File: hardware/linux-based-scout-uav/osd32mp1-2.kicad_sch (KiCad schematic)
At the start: 1 part, among them U1 OSD32MP157C-512M-IAA

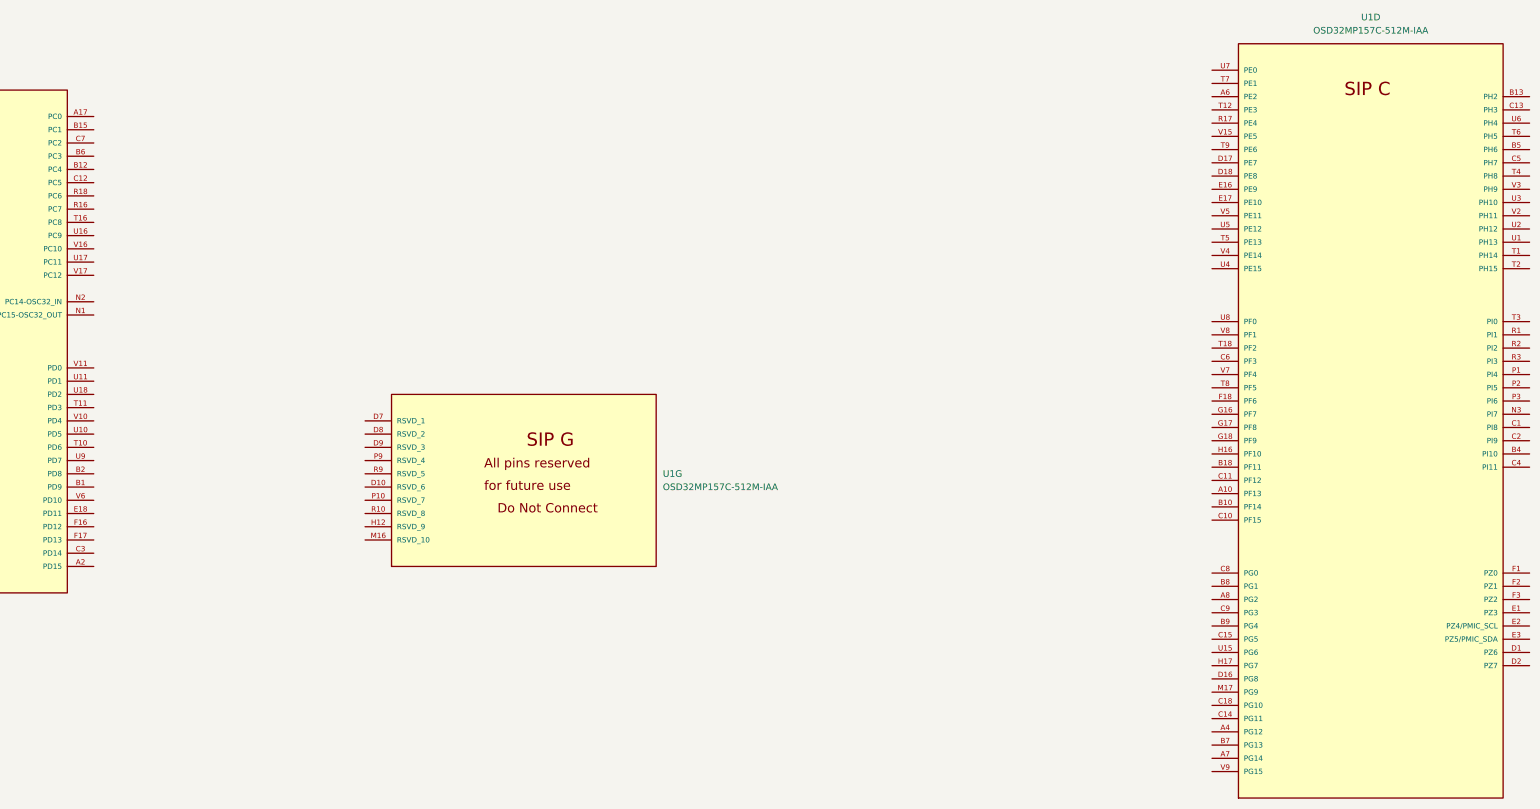
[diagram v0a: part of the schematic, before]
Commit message: Updates (Schematic, Readme, doc)
Updates to Schematic capture, README file and doc files.
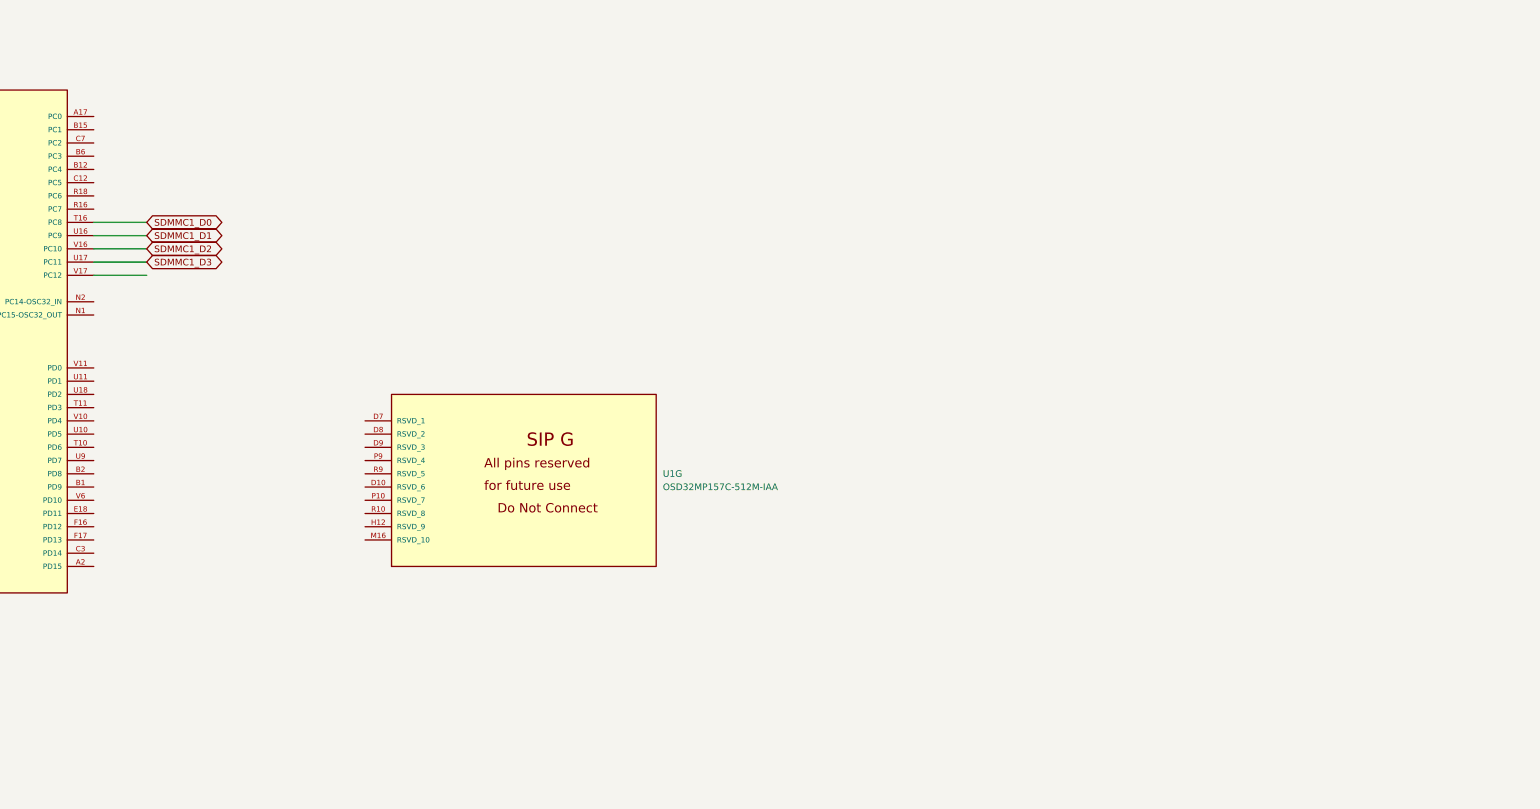
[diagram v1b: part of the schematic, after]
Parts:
- removed unit 4 of U1
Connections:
- net SDMMC1_D0: now reaches U1.T16 (PC8)
- net SDMMC1_D1: now reaches U1.U16 (PC9)
- net SDMMC1_D3: now reaches U1.U17 (PC11)
- net SDMMC1_D2: now reaches U1.V16 (PC10)

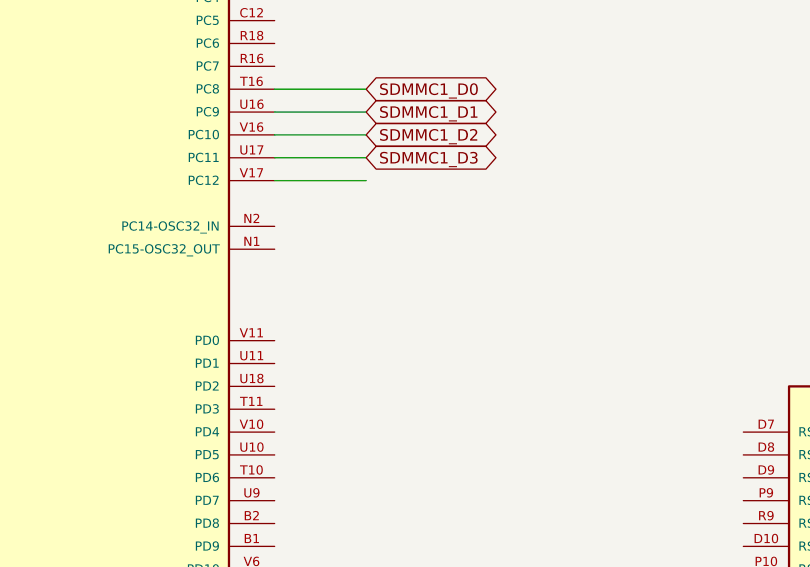
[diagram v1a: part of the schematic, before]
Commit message: Updates (schematic, readme, doc files, device tree)
Updates to schematic, readme file and doc files.
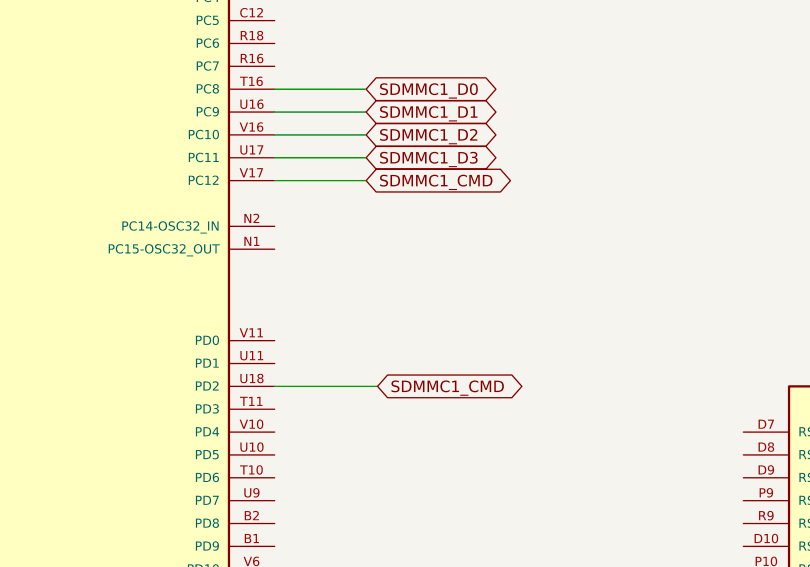
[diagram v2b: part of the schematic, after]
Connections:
- net SDMMC1_CMD: now reaches U1.U18 (PD2)
- net SDMMC1_CMD: now also U1.V17 (PC12)
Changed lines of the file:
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@@
 	(generator "eeschema")
 	(generator_version "8.0")
-	(paper "A4")
+	(paper "A3")
+	(wire
+		(pts
+			(xy 241.3 97.79) (xy 252.73 97.79)
+		)
+		(stroke
+			(width 0)
+			(type default)
+		)
+	)
 	(wire
 		(pts
@@
 			(width 0)
 			(type default)
+		)
+	)
+	(global_label "SDMMC1_CMD"
+		(shape bidirectional)
+		(at 251.46 74.93 0)
+		(fields_autoplaced yes)
+		(effects
+			(font
+				(size 1.27 1.27)
+			)
+			(justify left)
+		)
+		(property "Intersheetrefs" "${INTERSHEET_REFS}"
+			(at 268.3773 74.93 0)
+			(show_name yes)
+			(effects
+				(font
+					(size 1.27 1.27)
+				)
+				(justify left)
+				(hide yes)
+			)
 		)
 	)
@@
 			(effects
 				(font
+					(size 1.27 1.27)
+				)
+				(justify left)
+				(hide yes)
+			)
+		)
+	)
+	(global_label "SDMMC1_CMD"
+		(shape bidirectional)
+		(at 252.73 97.79 0)
+		(fields_autoplaced yes)
+		(effects
+			(font
+				(size 1.27 1.27)
+			)
+			(justify left)
+		)
+		(property "Intersheetrefs" "${INTERSHEET_REFS}"
+			(at 269.6473 97.79 0)
+			(show_name yes)
+			(effects
+				(font

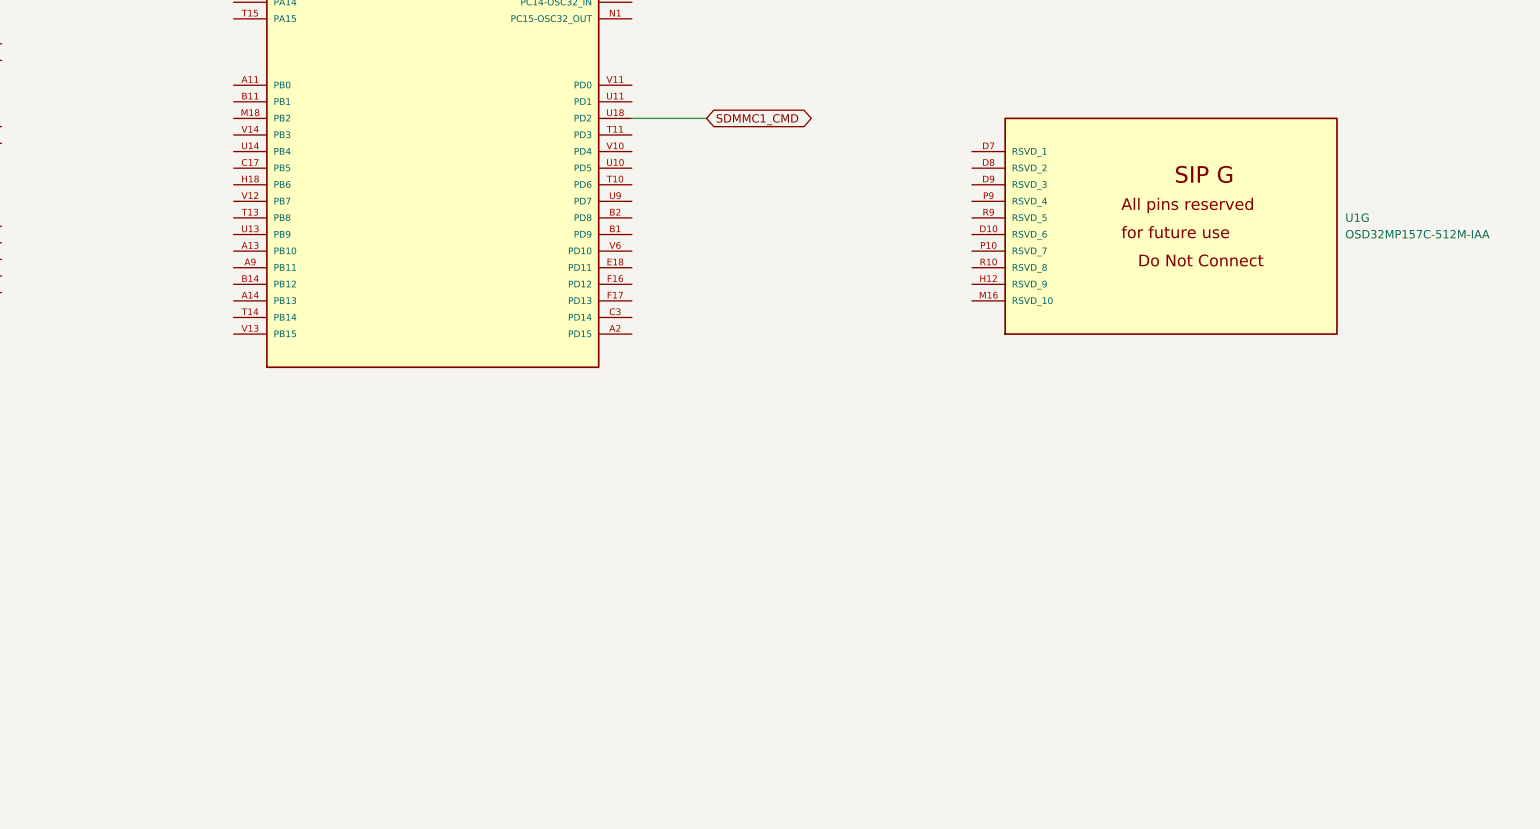
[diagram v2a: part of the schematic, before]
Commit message: schematic update
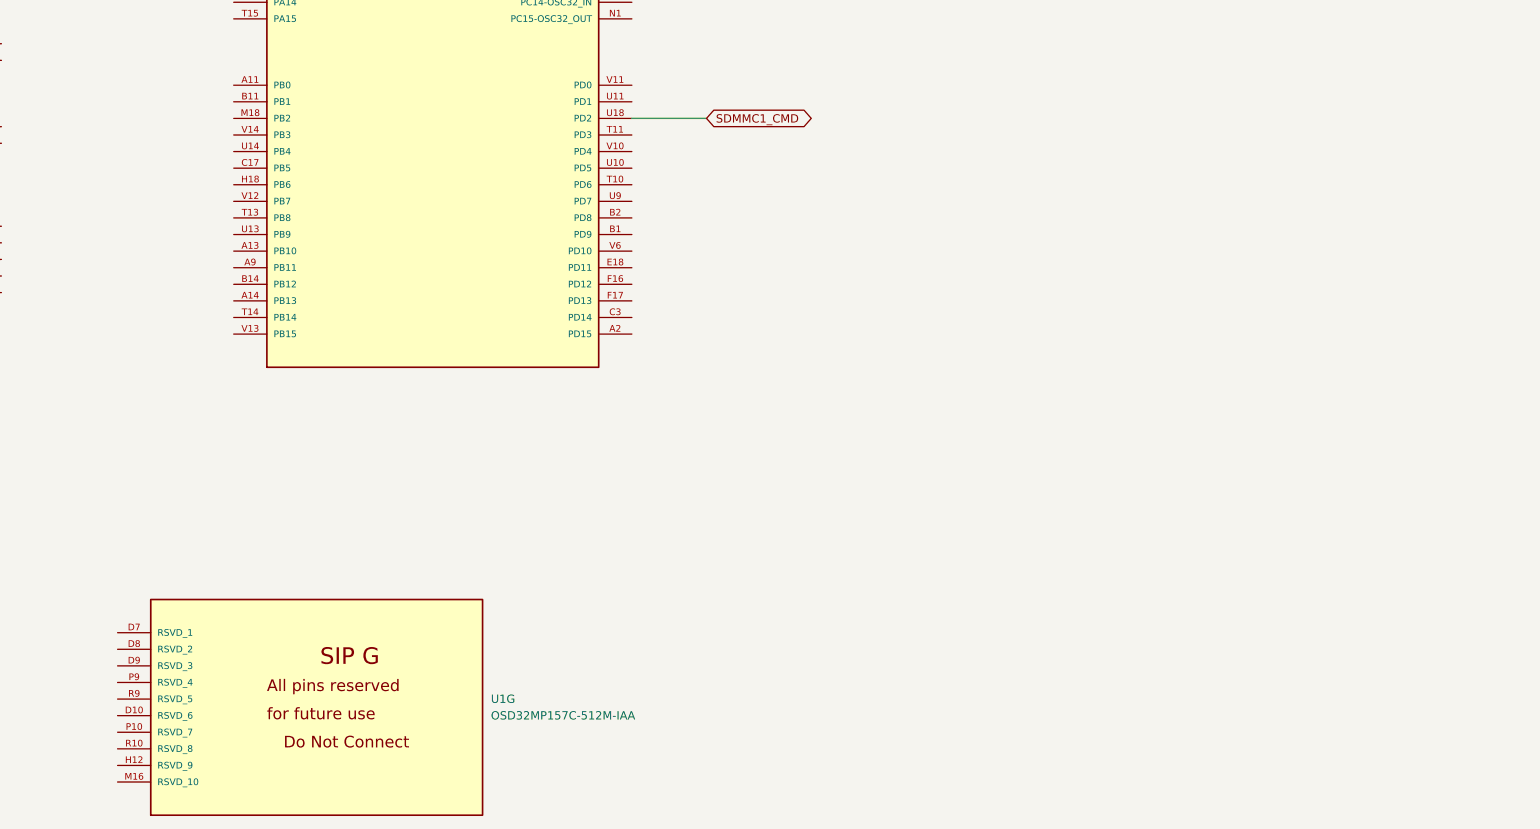
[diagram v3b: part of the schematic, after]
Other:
- moved on the sheet: U1G
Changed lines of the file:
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@@
 	(symbol
 		(lib_id "OSD32MP157C-512M-IAA:OSD32MP157C-512M-IAA")
-		(at 298.45 130.81 0)
+		(at 167.64 204.47 0)
 		(unit 7)
 		(exclude_from_sim no)
@@
 		(fields_autoplaced yes)
 		(property "Reference" "U1"
-			(at 350.52 113.0299 0)
+			(at 219.71 186.6899 0)
 			(effects
 				(font
@@
 		)
 		(property "Value" "OSD32MP157C-512M-IAA"
-			(at 350.52 115.5699 0)
+			(at 219.71 189.2299 0)
 			(effects
 				(font
@@
 		)
 		(property "Footprint" "OSD32MP157C-512M-IAA:OSD32MP15X-BGA-324"
-			(at 298.45 130.81 0)
+			(at 167.64 204.47 0)
 			(effects
 				(font
@@
 		)
 		(property "Datasheet" ""
-			(at 298.45 130.81 0)
+			(at 167.64 204.47 0)
 			(effects
 				(font
@@
 		)
 		(property "Description" ""
-			(at 298.45 130.81 0)
+			(at 167.64 204.47 0)
 			(effects
 				(font
@@
 		)
 		(property "MF" "Octavo Systems LLC"
-			(at 298.45 130.81 0)
+			(at 167.64 204.47 0)
 			(effects
 				(font
@@
 		)
 		(property "Description_1" "\nOSD32MP15x Embedded Module Arm® Dual Cortex®-A7, Arm® Cortex®-M4 NEON™ SIMD 650MHz, 209MHz\n"
-			(at 298.45 130.81 0)
+			(at 167.64 204.47 0)
 			(effects
 				(font
@@
 		)
 		(property "Package" "BGA-302 Octavo Systems"
-			(at 298.45 130.81 0)
+			(at 167.64 204.47 0)
 			(effects
 				(font
@@
 		)
 		(property "Price" "None"
-			(at 298.45 130.81 0)
+			(at 167.64 204.47 0)
 			(effects
 				(font
@@
 		)
 		(property "SnapEDA_Link" "https://www.snapeda.com/parts/OSD32MP157C-512M-IAA/Octavo+Systems+LLC/view-part/?ref=snap"
-			(at 298.45 130.81 0)
+			(at 167.64 204.47 0)
 			(effects
 				(font
@@
 		)
 		(property "MP" "OSD32MP157C-512M-IAA"
-			(at 298.45 130.81 0)
+			(at 167.64 204.47 0)
 			(effects
 				(font
@@
 		)
 		(property "Purchase-URL" "https://www.snapeda.com/api/url_track_click_mouser/?unipart_id=4998964&manufacturer=Octavo Systems LLC&part_name=OSD32MP157C-512M-IAA&search_term=osd32mp1"
-			(at 298.45 130.81 0)
+			(at 167.64 204.47 0)
 			(effects
 				(font
@@
 		)
 		(property "Availability" "In Stock"
-			(at 298.45 130.81 0)
+			(at 167.64 204.47 0)
 			(effects
 				(font
@@
 		)
 		(property "Check_prices" "https://www.snapeda.com/parts/OSD32MP157C-512M-IAA/Octavo+Systems+LLC/view-part/?ref=eda"
-			(at 298.45 130.81 0)
+			(at 167.64 204.47 0)
 			(effects
 				(font
